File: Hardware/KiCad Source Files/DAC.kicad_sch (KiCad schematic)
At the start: 14 parts, among them U4 LM4040LP-2.0, U5 MCP4801

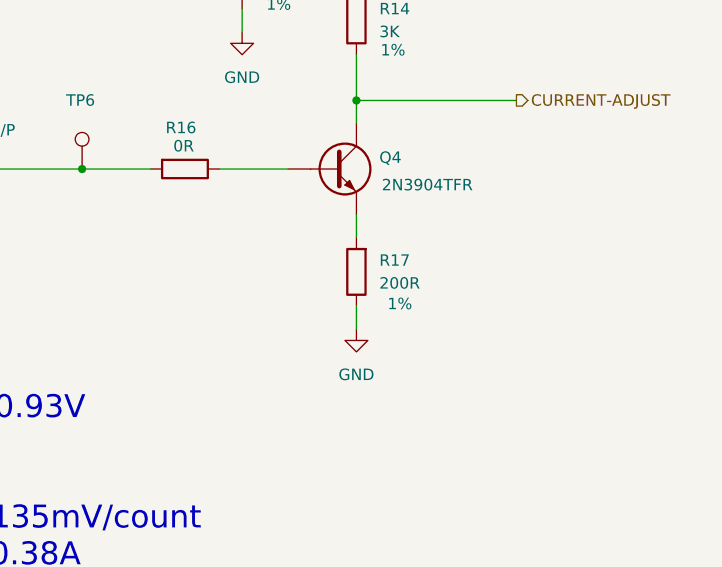
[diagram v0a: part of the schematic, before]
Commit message: Finalized V3 Connector BOM based on testing on hardware.
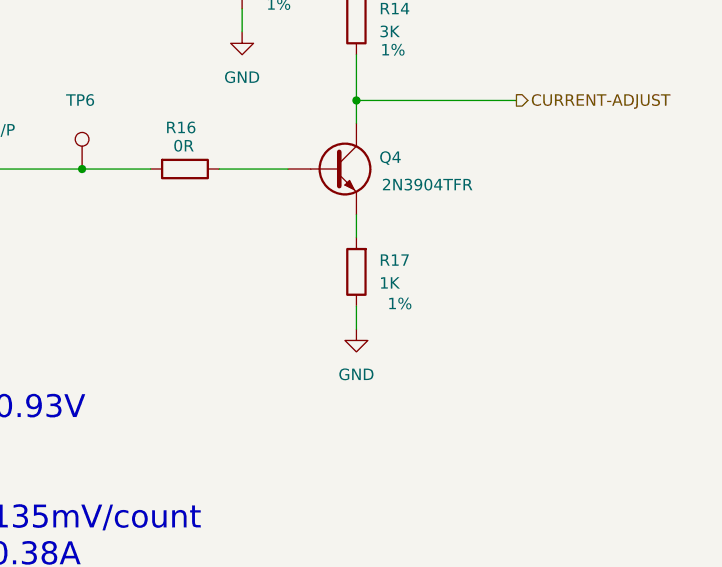
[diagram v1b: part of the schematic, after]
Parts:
- R17: value 200R -> 1K; Part Number MFR-25FRF52-200R -> MFR-25FRF52-1K
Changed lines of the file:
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@@
 			)
 		)
-		(property "Value" "200R"
+		(property "Value" "1K"
 			(at 203.2 126.9999 0)
 			(effects
@@
 			)
 		)
-		(property "Part Number" "MFR-25FRF52-200R"
+		(property "Part Number" "MFR-25FRF52-1K"
 			(at 200.66 125.73 90)
 			(effects
